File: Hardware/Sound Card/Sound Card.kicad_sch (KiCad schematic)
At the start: 35 parts, among them J1 ICSP, J2 6502 Card Edge, J3 Conn_02x08_Odd_Even, J4 PORT A, J5 3.5mm TRS, U1 ATmega328P-A, U2 74HC245, U3 74HC245, U4 74HC138, U5 AY-3-8912, U6 LM386, X1 2 MHz, Y1 16MHz

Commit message: Add Wozmon
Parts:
- removed C10, C2, C5, C6: 100nF, Capacitor_SMD:C_0805_2012Metric, symbol Device:C
- removed C11: 470nF, Capacitor_SMD:C_0805_2012Metric, symbol Device:C
- removed C3, C4: 22pF, Capacitor_SMD:C_0805_2012Metric, symbol Device:C
- removed D1: 1N4001, Diode_SMD:D_SMA, symbol Diode:1N4001
- removed J1: ICSP, Connector_PinHeader_2.54mm:PinHeader_2x03_P2.54mm_Vertical, symbol Connector_Generic:Conn_02x03_Odd_Even
- removed R4, R5, R6: 1k, Resistor_SMD:R_0805_2012Metric, symbol Device:R
- removed R7: 10, Resistor_SMD:R_0805_2012Metric, symbol Device:R
- removed U1: ATmega328P-A, Package_QFP:TQFP-32_7x7mm_P0.8mm, symbol MCU_Microchip_ATmega:ATmega328P-A
- removed U2, U3: 74HC245, Package_SO:SOIC-20W_7.5x12.8mm_P1.27mm, symbol 74xx:74HC245
- removed U6: LM386, Package_SO:SOP-8_3.76x4.96mm_P1.27mm, symbol Amplifier_Audio:LM386
- removed Y1: 16MHz, Crystal:Crystal_HC49-U_Vertical, symbol Device:Crystal
- added D1: D_Schottky, Diode_THT:D_DO-35_SOD27_P7.62mm_Horizontal, symbol Device:D_Schottky
- added J1: Audio Out, Connector_JST:JST_XH_B2B-XH-A_1x02_P2.50mm_Vertical, symbol Connector_Generic:Conn_01x02
- added JP1: SolderJumper_2_Bridged, Jumper:SolderJumper-2_P1.3mm_Bridged_RoundedPad1.0x1.5mm, symbol Jumper:SolderJumper_2_Bridged
- added U1: 65C22, Package_DIP:DIP-40_W15.24mm_Socket_LongPads, symbol 6502 Parts:65C22
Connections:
- net A0: now also U1.38 (RS0)
- net A1: now also U1.37 (RS1)
- net A2: now also U1.36 (RS2)
- net A3: now also U1.35 (RS3)
- net BC1: now also U1.10 (PB0)
- net BDIR: now also U1.11 (PB1)
- net CHOUT: now also U5.1 (CH_C), U5.4 (CH_B), U5.5 (CH_A)
- net CSB: now also U1.23 (CS2B)
- net D0: now also U1.33 (D0)
- net D1: now also U1.32 (D1)
- net D2: now also U1.31 (D2)
- net D3: now also U1.30 (D3)
- net D4: now also U1.29 (D4)
- net D5: now also U1.28 (D5)
- net D6: now also U1.27 (D6)
- net D7: now also U1.26 (D7)
- net DA0: now also U1.2 (PA0)
- net DA1: now also U1.3 (PA1)
- net DA2: now also U1.4 (PA2)
- net DA3: now also U1.5 (PA3)
- net DA4: now also U1.6 (PA4)
- net DA5: now also U1.7 (PA5)
- net DA6: now also U1.8 (PA6)
- net DA7: now also U1.9 (PA7)
- net GND: now also J5.R, J1.2 (Pin_2), U1.1 (VSS)
- net PHI2: now also U1.25 (PHI2)
- net RESB: now also U1.34 (RESB); no longer U5.16 (~{RESET})
- net VCC: now also U1.20 (VDD), U1.24 (CS1)
- net at C9.2: now also J5.T, TP2.1, J1.1 (Pin_1)
- net CA1: now reaches J4.11 (Pin_11)
- net CA1: now also U1.40 (CA1)
- net CA2: now reaches J4.12 (Pin_12)
- net CA2: now also U1.39 (CA2)
- net IRQB: now reaches J2.IRQB
- net IRQB: now also D1.2 (A), JP1.2 (B)
- net MISO renamed RWB
- net RWB: now also U1.22 (RWB)
- new net: D1.1 (K), JP1.1 (A), U1.21 (IRQB)
- new net RESETB: U1.12 (PB2), U5.16 (~{RESET})
- no-connect marks 25 -> 23
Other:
- moved on the sheet: C7, C8, C9, J2, J3, J4, J5, R1, R2, R3, TP1, TP2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

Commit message: Cleanup
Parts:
- removed J5: 3.5mm TRS, Connector_Audio:Jack_3.5mm_CUI_SJ1-3523N_Horizontal, symbol Connector_Audio:AudioJack3
- added C3: 100nF, Capacitor_SMD:C_0805_2012Metric, symbol Device:C
- added J4: Audio Out, 6502 Parts:SWITCHCRAFT_PJRAN1X1U02X, symbol 6502 Parts:PJRAN1X1U02X
- TP2: renamed from TP1; value Audio Raw -> Mixer
- renumbered C7 to C2, C8 to C4, C9 to C5, J2 to J1, J3 to J2, J4 to J3, J1 to J5, TP3 to TP1, TP2 to TP3, U4 to U2, U5 to U3
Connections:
- net GND: now also C3.2, J4.1 (Ext)
- net VCC: now also C3.1
- net at C5.2, J5.1 (Pin_1), TP3.1: now also J4.2 (In)
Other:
- moved on the sheet: J5, TP3

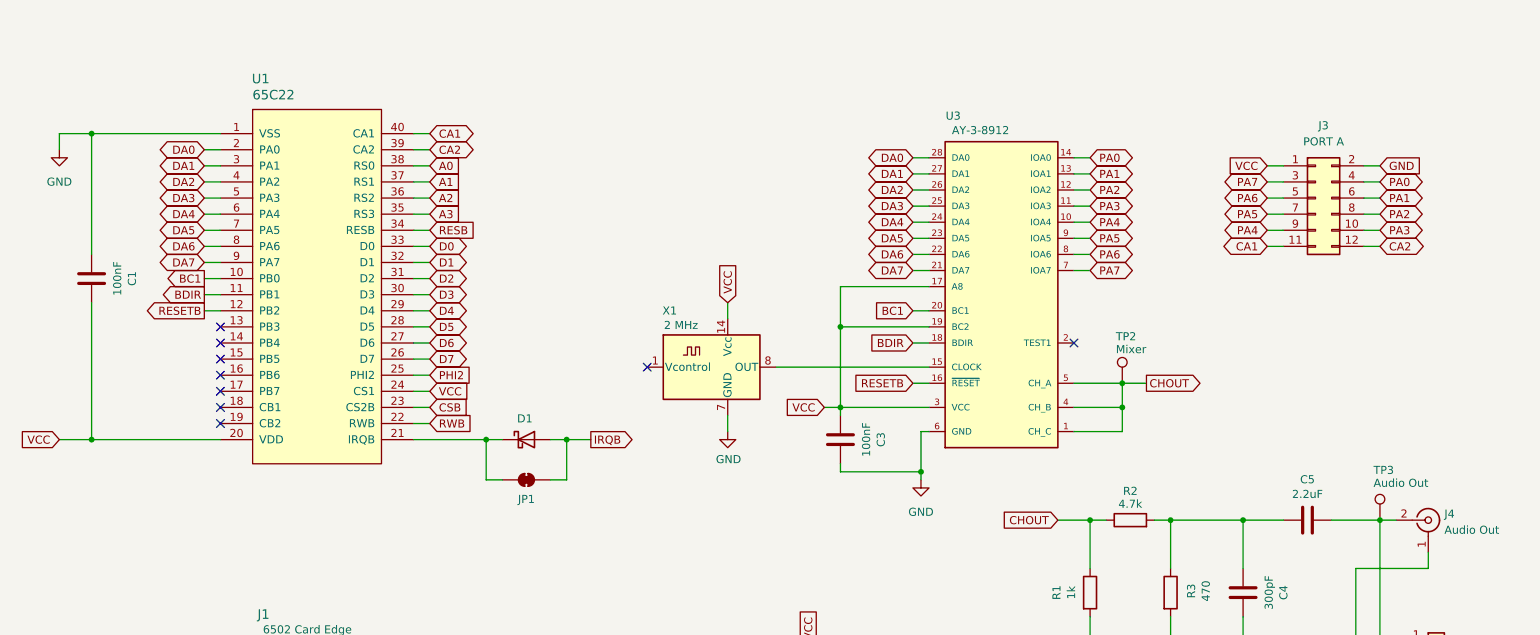
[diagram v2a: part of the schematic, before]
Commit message: Add Input Board and rework Debugger
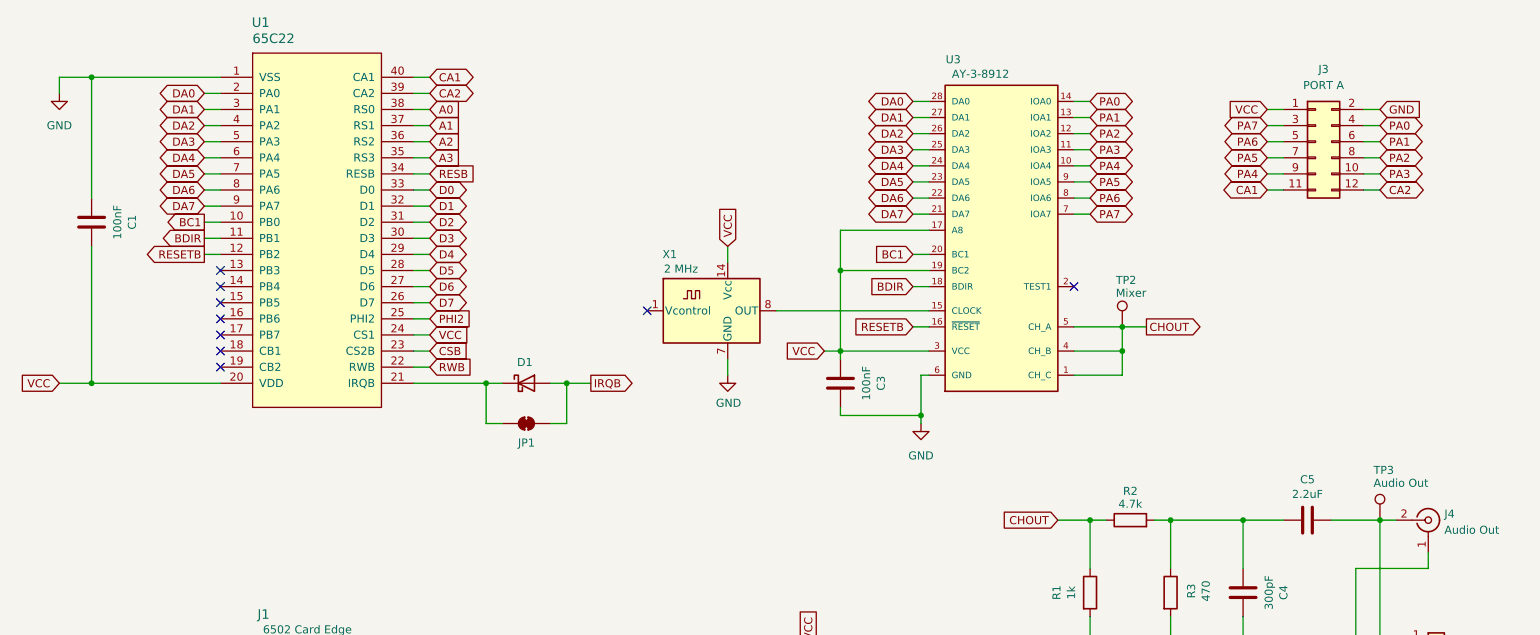
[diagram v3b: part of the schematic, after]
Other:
- moved on the sheet: C1, C3, D1, J3, JP1, TP2, U1, U3, X1

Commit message: Revise some boards
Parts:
- added J2: PHI2, Connector_PinHeader_2.54mm:PinHeader_1x02_P2.54mm_Vertical, symbol Connector_Generic:Conn_01x02
- renumbered J2 to J3, J3 to J4, J4 to J5, J5 to J6
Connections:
- net PHI2: now also J2.1 (Pin_1)
- net at U3.15 (CLOCK), X1.8 (OUT): now also J2.2 (Pin_2)
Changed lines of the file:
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@@
 	(title_block
 		(title "6502 Sound Card")
-		(date "2024-06-16")
+		(date "2024-06-19")
 		(rev "1.0")
 		(company "A.C. Wright Design")
@@
 	)
 	(junction
+		(at 139.7 73.66)
+		(diameter 0)
+		(color 0 0 0 0)
+	)
+	(junction
 		(at 180.34 151.13)
 		(diameter 0)
@@
 	(wire
 		(pts
-			(xy 135.89 73.66) (xy 160.02 73.66)
+			(xy 135.89 73.66) (xy 139.7 73.66)
 		)
 		(stroke
@@
 	(wire
 		(pts
+			(xy 139.7 73.66) (xy 160.02 73.66)
+		)
+		(stroke
+			(width 0)
+			(type default)
+		)
+	)
+	(wire
+		(pts
 			(xy 157.48 50.8) (xy 160.02 50.8)
 		)
@@
 	(wire
 		(pts
+			(xy 139.7 52.07) (xy 139.7 73.66)
+		)
+		(stroke
+			(width 0)
+			(type default)
+		)
+	)
+	(wire
+		(pts
 			(xy 78.74 36.83) (xy 81.28 36.83)
 		)
@@
 	(wire
 		(pts
+			(xy 137.16 49.53) (xy 139.7 49.53)
+		)
+		(stroke
+			(width 0)
+			(type default)
+		)
+	)
+	(wire
+		(pts
 			(xy 27.94 36.83) (xy 27.94 55.88)
 		)
@@
 		)
 	)
+	(global_label "PHI2"
+		(shape input)
+		(at 137.16 49.53 180)
+		(effects
+			(font
+				(size 1.27 1.27)
+			)
+			(justify right)
+		)
+		(property "Intersheetrefs" "${INTERSHEET_REFS}"
+			(at 137.16 49.53 0)
+			(effects
+				(font
+					(size 1.27 1.27)
+				)
+				(hide yes)
+			)
+		)
+	)
 	(global_label "PA6"
 		(shape bidirectional)
@@
 		(dnp no)
 		(fields_autoplaced yes)
-		(property "Reference" "J4"
+		(property "Reference" "J5"
 			(at 241.3 105.7031 0)
 			(effects
@@
 			(project ""
 				(path "/154a5133-b84f-49cb-b657-9c810539146c"
-					(reference "J4")
+					(reference "J5")
 					(unit 1)
 				)
@@
 		(on_board yes)
 		(dnp no)
-		(property "Reference" "J2"
+		(property "Reference" "J3"
 			(at 171.45 140.335 0)
 			(effects
@@
 			(project "Pi Card"
 				(path "/154a5133-b84f-49cb-b657-9c810539146c"
-					(reference "J2")
+					(reference "J3")
 					(unit 1)
 				)
@@
 	)
 	(symbol
+		(lib_id "Connector_Generic:Conn_01x02")
+		(at 144.78 49.53 0)
+		(unit 1)
+		(exclude_from_sim no)
+		(in_bom yes)
+		(on_board yes)
+		(dnp no)
+		(property "Reference" "J2"
+			(at 146.558 43.942 0)
+			(effects
+				(font
+					(size 1.27 1.27)
+				)
+				(justify right)
+			)
+		)
+		(property "Value" "PHI2"
+			(at 146.558 46.228 0)
+			(effects
+				(font
+					(size 1.27 1.27)
+				)
+				(justify right)
+			)
+		)
+		(property "Footprint" "Connector_PinHeader_2.54mm:PinHeader_1x02_P2.54mm_Vertical"
+			(at 144.78 49.53 0)
+			(effects
+				(font
+					(size 1.27 1.27)
+				)
+				(hide yes)
+			)
+		)
+		(property "Datasheet" "~"
+			(at 144.78 49.53 0)
+			(effects
+				(font
+					(size 1.27 1.27)
+				)
+				(hide yes)
+			)
+		)
+		(property "Description" "Generic connector, single row, 01x02, script generated (kicad-library-utils/schlib/autogen/connector/)"
+			(at 144.78 49.53 0)
+			(effects
+				(font
+					(size 1.27 1.27)
+				)
+				(hide yes)
+			)
+		)
+		(pin "2"
+		)
+		(pin "1"
+		)
+		(instances
+			(project "Sound Card"
+				(path "/154a5133-b84f-49cb-b657-9c810539146c"
+					(reference "J2")
+					(unit 1)
+				)
+			)
+		)
+	)
+	(symbol
 		(lib_id "Connector_Generic:Conn_02x06_Odd_Even")
 		(at 220.98 46.99 0)
@@
 		(dnp no)
 		(fields_autoplaced yes)
-		(property "Reference" "J3"
+		(property "Reference" "J4"
 			(at 222.25 35.56 0)
 			(effects
@@
 			(project "Sound Card"
 				(path "/154a5133-b84f-49cb-b657-9c810539146c"
-					(reference "J3")
+					(reference "J4")
 					(unit 1)
 				)
@@
 		(dnp no)
 		(fields_autoplaced yes)
-		(property "Reference" "J5"
+		(property "Reference" "J6"
 			(at 242.57 125.7299 0)
 			(effects
@@
 			(project ""
 				(path "/154a5133-b84f-49cb-b657-9c810539146c"
-					(reference "J5")
+					(reference "J6")
 					(unit 1)
 				)

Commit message: More PCBs
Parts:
- J2, J6, TP1, TP2, TP3: now left out of the parts list
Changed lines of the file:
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@@
 		(unit 1)
 		(exclude_from_sim no)
-		(in_bom yes)
+		(in_bom no)
 		(on_board yes)
 		(dnp no)
@@
 		(unit 1)
 		(exclude_from_sim no)
-		(in_bom yes)
+		(in_bom no)
 		(on_board yes)
 		(dnp no)
@@
 		(unit 1)
 		(exclude_from_sim no)
-		(in_bom yes)
+		(in_bom no)
 		(on_board yes)
 		(dnp no)
@@
 		(unit 1)
 		(exclude_from_sim no)
-		(in_bom yes)
+		(in_bom no)
 		(on_board yes)
 		(dnp no)
@@
 		(unit 1)
 		(exclude_from_sim no)
-		(in_bom yes)
-		(on_board yes)
-		(dnp no)
+		(in_bom no)
+		(on_board yes)
+		(dnp no)
